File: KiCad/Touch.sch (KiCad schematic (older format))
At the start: 11 parts, among them P1 CONN_01X10, P2 CONN_01X05, P3 CONN_01X04, U1 MTCH6102_SSOP28

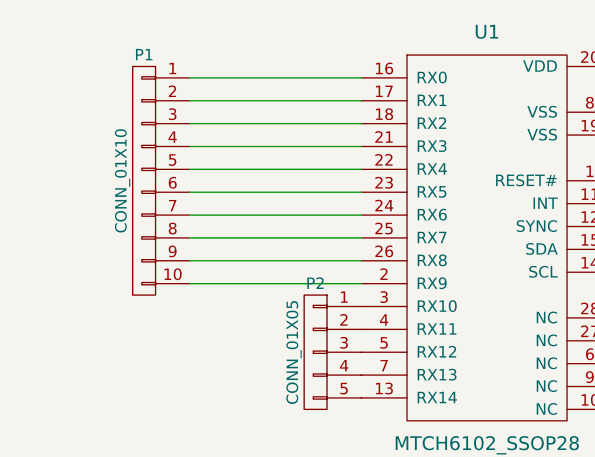
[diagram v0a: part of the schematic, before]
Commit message: add FPC connector.
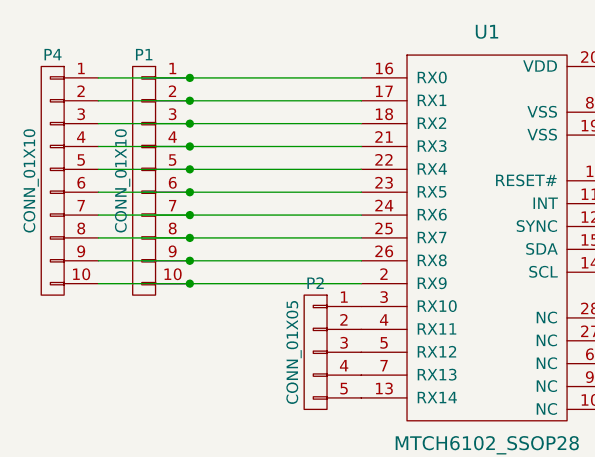
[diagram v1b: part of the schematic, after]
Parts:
- added P4: CONN_01X10, library:FFC_CONNECTOR_1.0D-WTS-10P, symbol CONN_01X10
- U1: footprint Housings_SSOP:TSSOP-28_4.4x9.7mm_Pitch0.65mm -> Housings_SSOP:SSOP-28_5.3x10.2mm_Pitch0.65mm
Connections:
- net at P1.1 (P1), U1.16 (RX0): now also P4.1 (P1)
- net at P1.2 (P2), U1.17 (RX1): now also P4.2 (P2)
- net at P1.3 (P3), U1.18 (RX2): now also P4.3 (P3)
- net at P1.10 (P10), U1.2 (RX9): now also P4.10 (P10)
- net at P1.4 (P4), U1.21 (RX3): now also P4.4 (P4)
- net at P1.5 (P5), U1.22 (RX4): now also P4.5 (P5)
- net at P1.6 (P6), U1.23 (RX5): now also P4.6 (P6)
- net at P1.7 (P7), U1.24 (RX6): now also P4.7 (P7)
- net at P1.8 (P8), U1.25 (RX7): now also P4.8 (P8)
- net at P1.9 (P9), U1.26 (RX8): now also P4.9 (P9)
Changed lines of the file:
@@
 F 0 "U1" H 5500 5300 60  0000 C CNN
 F 1 "MTCH6102_SSOP28" H 5500 3500 60  0000 C CNN
-F 2 "Housings_SSOP:TSSOP-28_4.4x9.7mm_Pitch0.65mm" H 5400 4400 60  0001 C CNN
+F 2 "Housings_SSOP:SSOP-28_5.3x10.2mm_Pitch0.65mm" H 5400 4400 60  0001 C CNN
 F 3 "" H 5400 4400 60  0000 C CNN
 	1    5500 4400
@@
 $EndComp
 Wire Wire Line
-	4200 3700 4950 3700
-Wire Wire Line
-	4200 3800 4950 3800
-Wire Wire Line
-	4200 3900 4950 3900
-Wire Wire Line
-	4200 4000 4950 4000
-Wire Wire Line
-	4200 4100 4950 4100
-Wire Wire Line
-	4200 4200 4950 4200
-Wire Wire Line
-	4200 4300 4950 4300
-Wire Wire Line
-	4200 4400 4950 4400
-Wire Wire Line
-	4200 4500 4950 4500
-Wire Wire Line
-	4200 4600 4950 4600
+	3800 3700 4950 3700
+Wire Wire Line
+	3800 3800 4950 3800
+Wire Wire Line
+	3800 3900 4950 3900
+Wire Wire Line
+	3800 4000 4950 4000
+Wire Wire Line
+	3800 4100 4950 4100
+Wire Wire Line
+	3800 4200 4950 4200
+Wire Wire Line
+	3800 4300 4950 4300
+Wire Wire Line
+	3800 4400 4950 4400
+Wire Wire Line
+	3800 4500 4950 4500
+Wire Wire Line
+	3800 4600 4950 4600
 $Comp
 L CONN_01X05 P2
@@
 	7750 4350 7750 3650
 Connection ~ 7550 3650
+$Comp
+L CONN_01X10 P4
+U 1 1 5B446E65
+P 3600 4150
+F 0 "P4" H 3600 4700 50  0000 C CNN
+F 1 "CONN_01X10" V 3700 4150 50  0000 C CNN
+F 2 "library:FFC_CONNECTOR_1.0D-WTS-10P" H 3600 4150 50  0001 C CNN
+F 3 "" H 3600 4150 50  0000 C CNN
+	1    3600 4150
+	-1   0    0    -1
+$EndComp
+Connection ~ 4200 3700
+Connection ~ 4200 3800
+Connection ~ 4200 3900
+Connection ~ 4200 4000
+Connection ~ 4200 4100
+Connection ~ 4200 4200
+Connection ~ 4200 4300
+Connection ~ 4200 4400
+Connection ~ 4200 4500
+Connection ~ 4200 4600
 $EndSCHEMATC
